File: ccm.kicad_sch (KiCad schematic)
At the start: 27 parts, among them J3 Conn_01x04_Socket, J4 Conn_01x04_Socket, J5 Conn_01x04_Socket, J6 Conn_01x02_Socket, J7 Conn_01x02_Socket, J8 Conn_01x04_Socket, Q1 IRLZ34N, U1 Teensy4.1, U2 PAM8302AAY, U3 SN65HVD230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

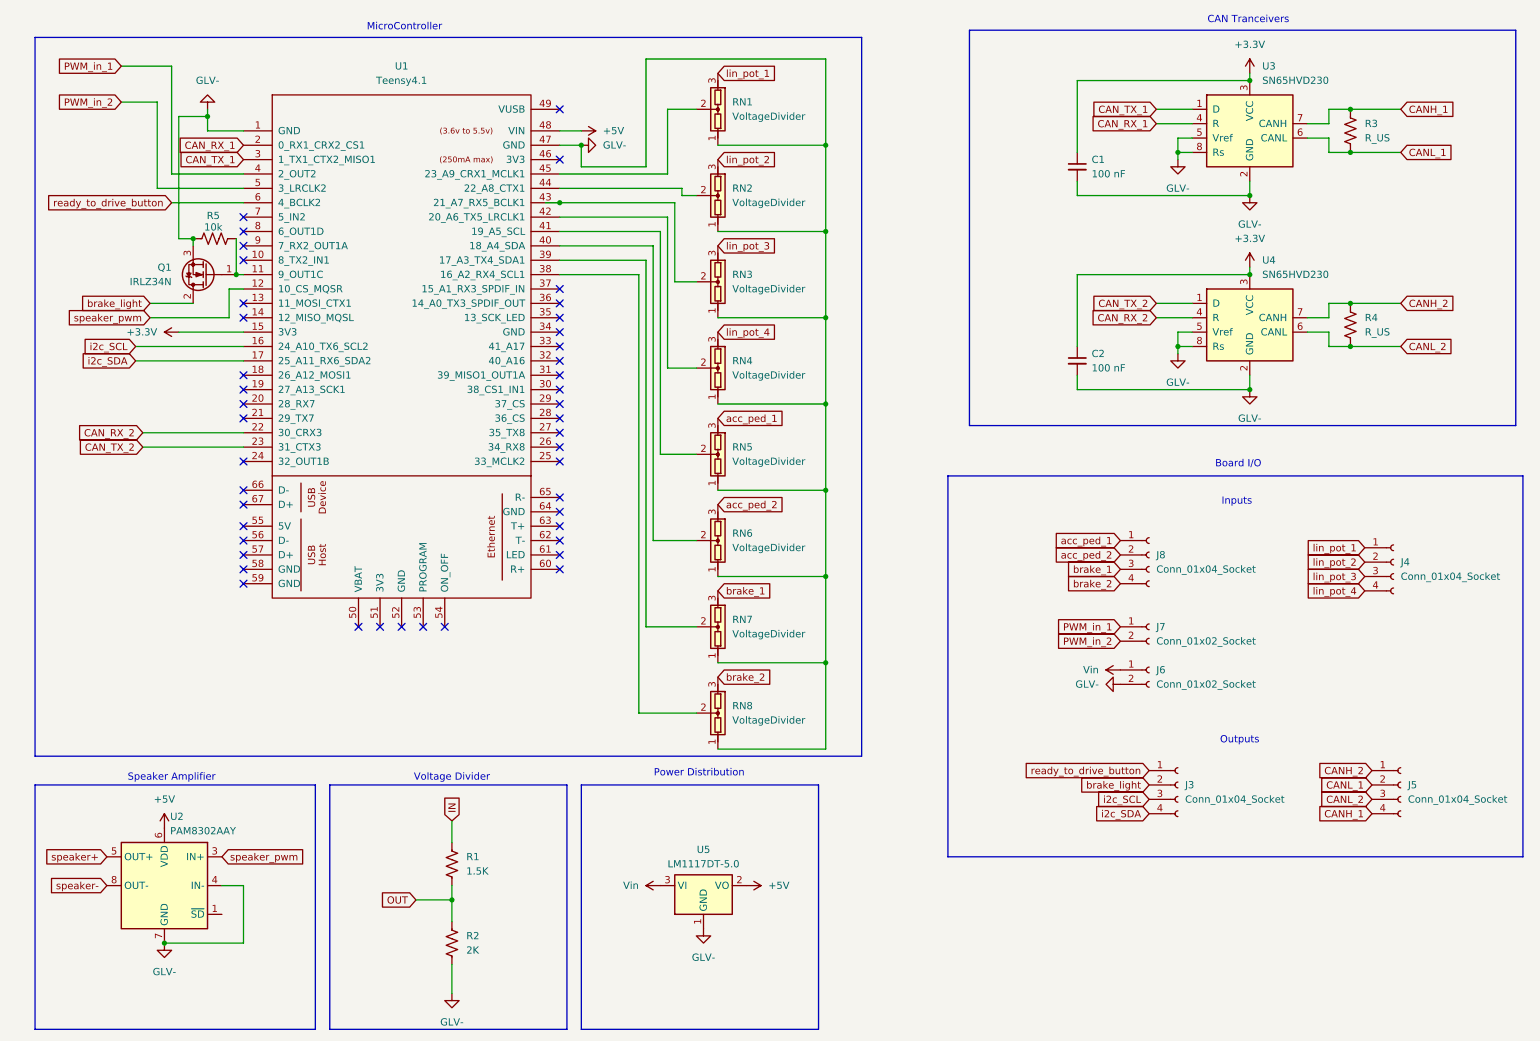
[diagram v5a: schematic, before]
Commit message: changed voltage divider to use 2 resistors
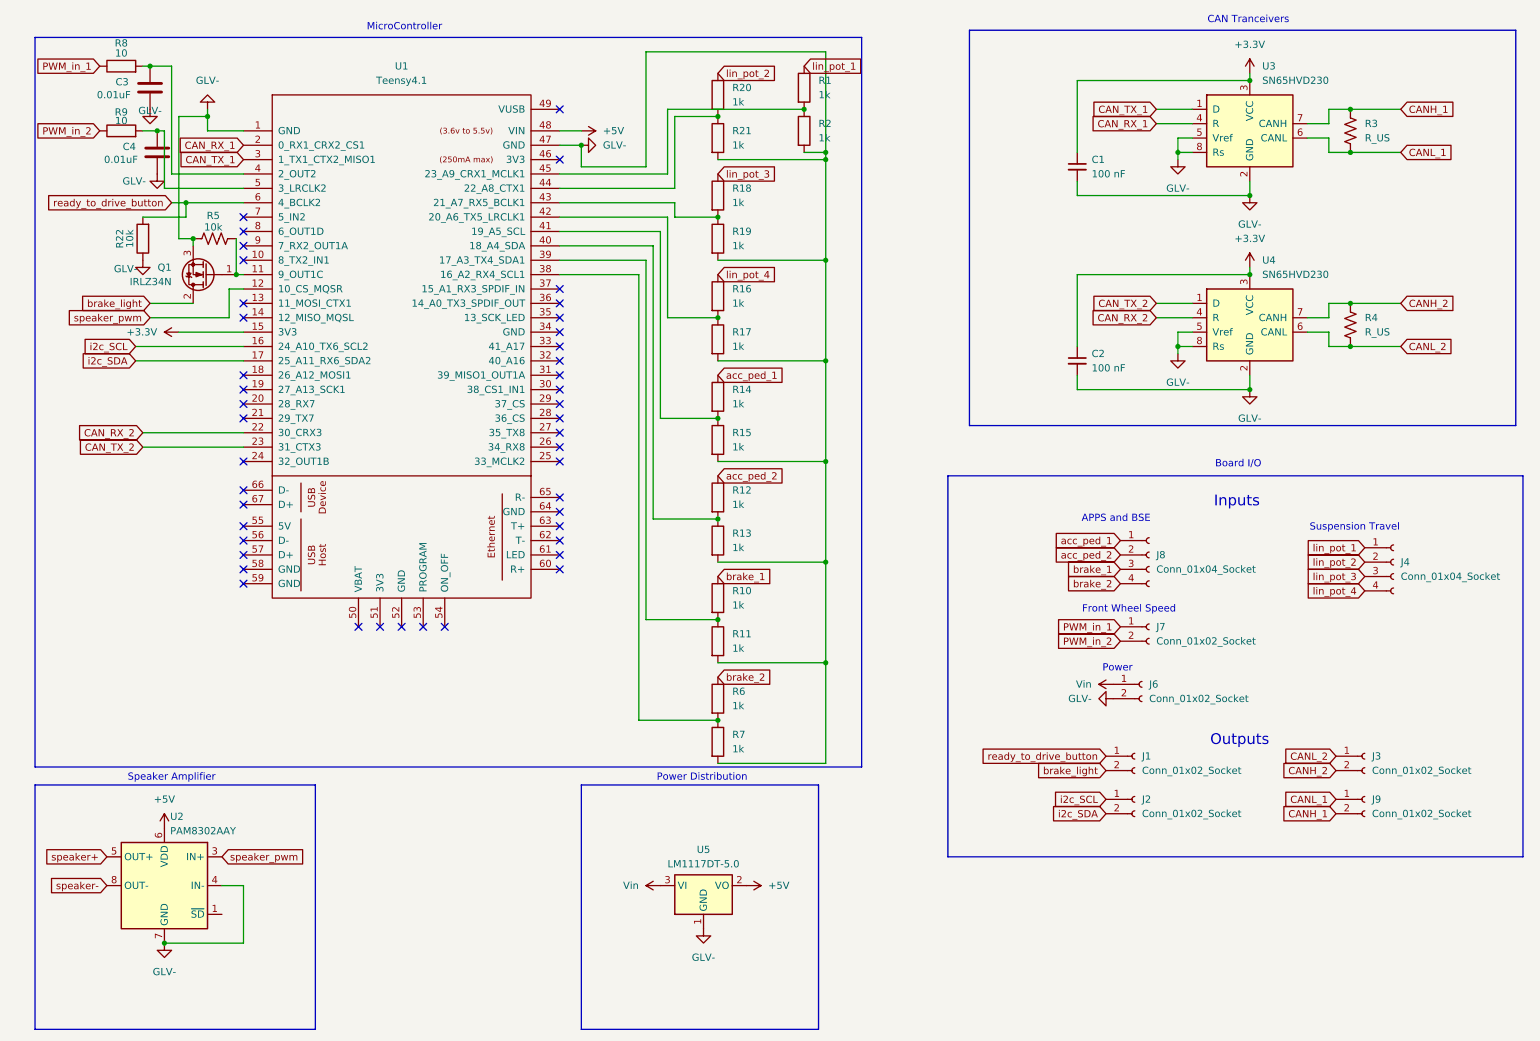
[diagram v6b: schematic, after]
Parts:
- removed J3, J5: Conn_01x04_Socket, Connector_Molex:Molex_Mini-Fit_Jr_5566-04A2_2x02_P4.20mm_Vertical, symbol Connector:Conn_01x04_Socket
- removed R1: 1.5K, symbol Device:R_US
- removed R2: 2K, symbol Device:R_US
- removed RN1, RN2, RN3, RN4, RN5, RN6, RN7, RN8: VoltageDivider, voltagedivider:Voltage_Divider, symbol Device:VoltageDivider
- added C3, C4: 0.01uF, Capacitor_SMD:C_0805_2012Metric, symbol Device:C
- added J1, J2, J3, J9: Conn_01x02_Socket, Connector_Molex:Molex_Mini-Fit_Jr_5566-02A2_2x01_P4.20mm_Vertical, symbol Connector:Conn_01x02_Socket
- added R1, R10, R11, R12, R13, R14, R15, R16, R17, R18, R19, R2, R20, R21, R6, R7: 1k, Resistor_SMD:R_0805_2012Metric, symbol Device:R
- added R22: 10k, Resistor_SMD:R_0805_2012Metric, symbol Device:R
- added R8, R9: 10, Resistor_SMD:R_0805_2012Metric, symbol Device:R
- C1, C2: footprint (none) -> Capacitor_SMD:C_0805_2012Metric
- R3, R4: footprint (none) -> Resistor_SMD:R_0805_2012Metric
- R5: footprint Resistor_SMD:R_0805_2012Metric_Pad1.20x1.40mm_HandSolder -> Resistor_SMD:R_0805_2012Metric
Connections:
- net CANH_1: now also J9.2 (Pin_2)
- net CANH_2: now also J3.2 (Pin_2)
- net CANL_1: now also J9.1 (Pin_1)
- net CANL_2: now also J3.1 (Pin_1)
- net GLV-: now also C3.2, C4.2, R11.2, R13.2, R15.2, R17.2, R19.2, R2.2, R21.2, R22.1, R7.2
- net PWM_in_1: now also R8.1; no longer U1.4 (2_OUT2)
- net PWM_in_2: now also R9.1; no longer U1.5 (3_LRCLK2)
- net acc_ped_1: now also R14.1
- net acc_ped_2: now also R12.1
- net brake_1: now also R10.1
- net brake_2: now also R6.1
- net brake_light: now also J1.2 (Pin_2)
- net i2c_SCL: now also J2.1 (Pin_1)
- net i2c_SDA: now also J2.2 (Pin_2)
- net lin_pot_1: now also R1.1
- net lin_pot_2: now also R20.1
- net lin_pot_3: now also R18.1
- net lin_pot_4: now also R16.1
- net ready_to_drive_button: now also J1.1 (Pin_1), R22.2
- net at U1.42 (20_A6_TX5_LRCLK1): now also R16.2, R17.1
- net at U1.40 (18_A4_SDA): now also R12.2, R13.1
- net at U1.43 (21_A7_RX5_BCLK1): now also R18.2, R19.1
- net at U1.41 (19_A5_SCL): now also R14.2, R15.1
- net at U1.44 (22_A8_CTX1): now also R20.2, R21.1
- net at U1.39 (17_A3_TX4_SDA1): now also R10.2, R11.1
- net at U1.38 (16_A2_RX4_SCL1): now also R6.2, R7.1
- net at U1.45 (23_A9_CRX1_MCLK1): now also R1.2, R2.1
- new net: C3.1, R8.2, U1.4 (2_OUT2)
- new net: C4.1, R9.2, U1.5 (3_LRCLK2)
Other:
- note added: "APPS and BSE"
- note added: "Front Wheel Speed"
- note added: "Power"
- note added: "Suspension Travel"
- note removed: "Voltage Divider"
- moved on the sheet: J6

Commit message: right side routed
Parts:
- added C5, C6: 100 nF, Capacitor_SMD:C_0805_2012Metric, symbol Device:C_Small
- added J10, J5: Conn_01x02_Socket, Connector_Molex:Molex_Mini-Fit_Jr_5566-02A2_2x01_P4.20mm_Vertical, symbol Connector:Conn_01x02_Socket
- added R23, R24: 1k, Resistor_SMD:R_0805_2012Metric, symbol Device:R
- added R25, R26: 60, Resistor_SMD:R_0805_2012Metric, symbol Device:R_US
- R3, R4: value R_US -> 60
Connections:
- net CANL_1: now also R25.2; no longer R3.2
- net CANL_2: now also R26.2; no longer R4.2
- net GLV-: now also C5.2, C6.2, R24.2
- net acc_ped_1: now also J8.4 (Pin_4); no longer J8.1 (Pin_1)
- net acc_ped_2: now also J8.3 (Pin_3); no longer J8.2 (Pin_2)
- net brake_1: now also J8.2 (Pin_2); no longer J8.3 (Pin_3)
- net brake_2: now also J8.1 (Pin_1); no longer J8.4 (Pin_4)
- net lin_pot_1: now also J4.4 (Pin_4); no longer J4.1 (Pin_1)
- net lin_pot_2: now also J4.3 (Pin_3); no longer J4.2 (Pin_2)
- net lin_pot_3: now also J4.2 (Pin_2); no longer J4.3 (Pin_3)
- net lin_pot_4: now also J4.1 (Pin_1); no longer J4.4 (Pin_4)
- net speaker+: now also J10.1 (Pin_1)
- net speaker-: now also J10.2 (Pin_2)
- net at U1.37 (15_A1_RX3_SPDIF_IN): now also R23.2, R24.1
- new net: C6.1, R26.1, R4.2
- new net: C5.1, R25.1, R3.2
- new net rtm_sound: J5.1 (Pin_1), R23.1
- no-connect marks 44 -> 45
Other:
- moved on the sheet: C3, C4, J3, J9, Q1, R22, R3, R5, R8, R9, U1

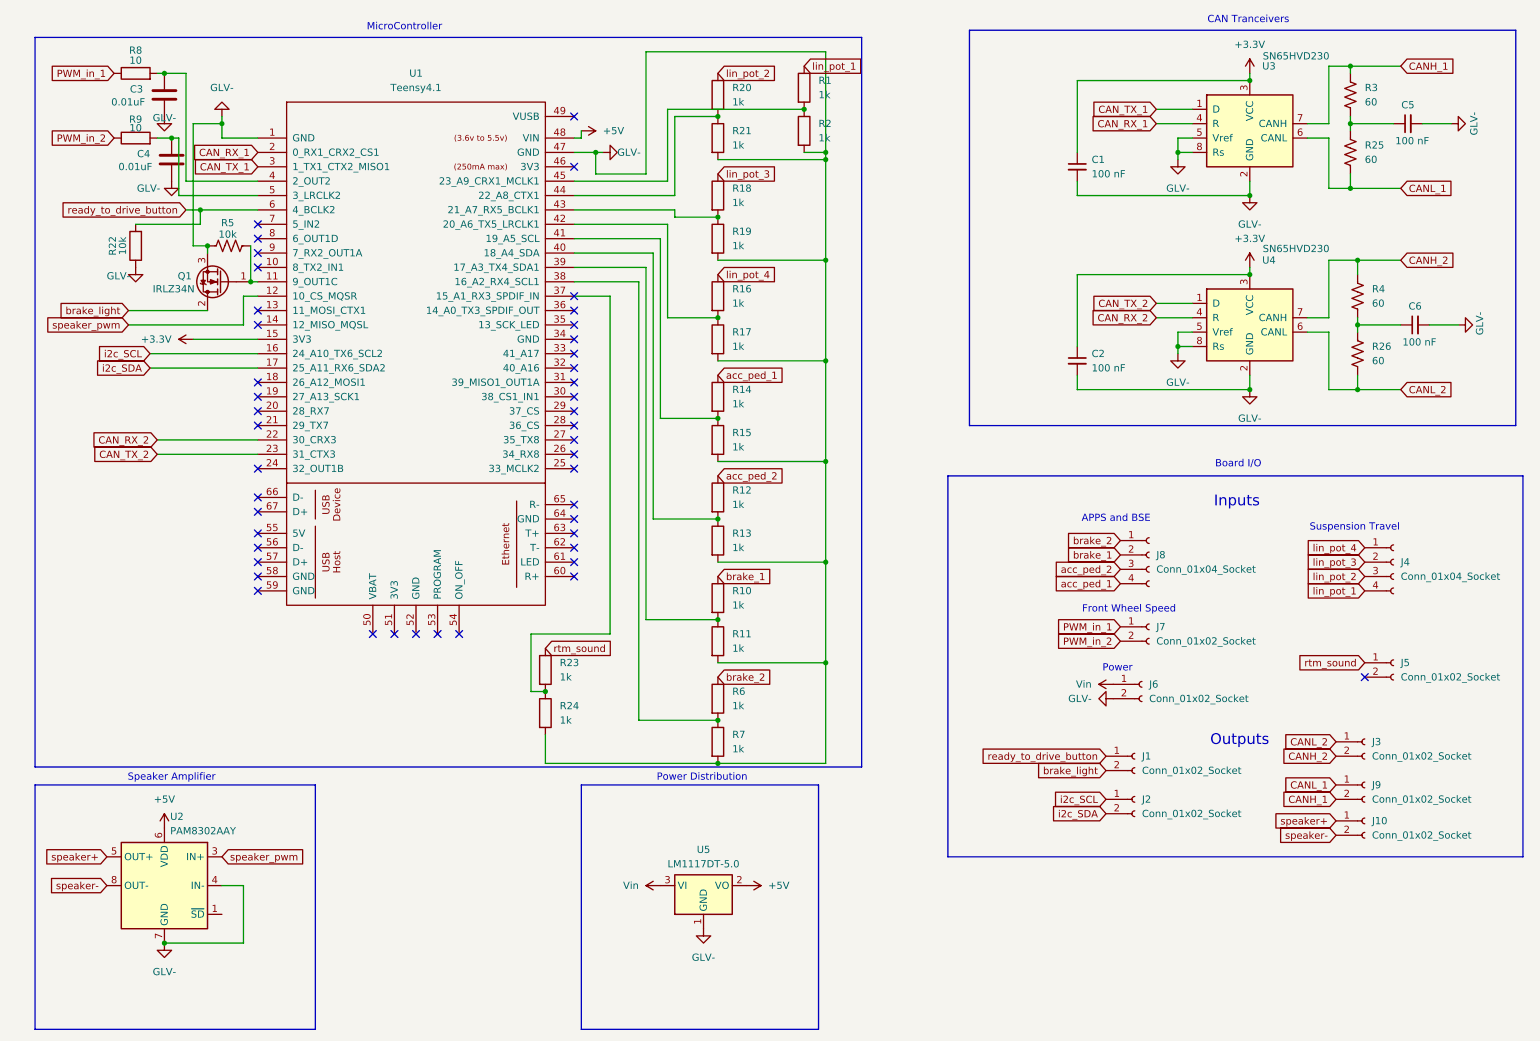
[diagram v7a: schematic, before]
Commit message: added serial resistors to CAN tranciever
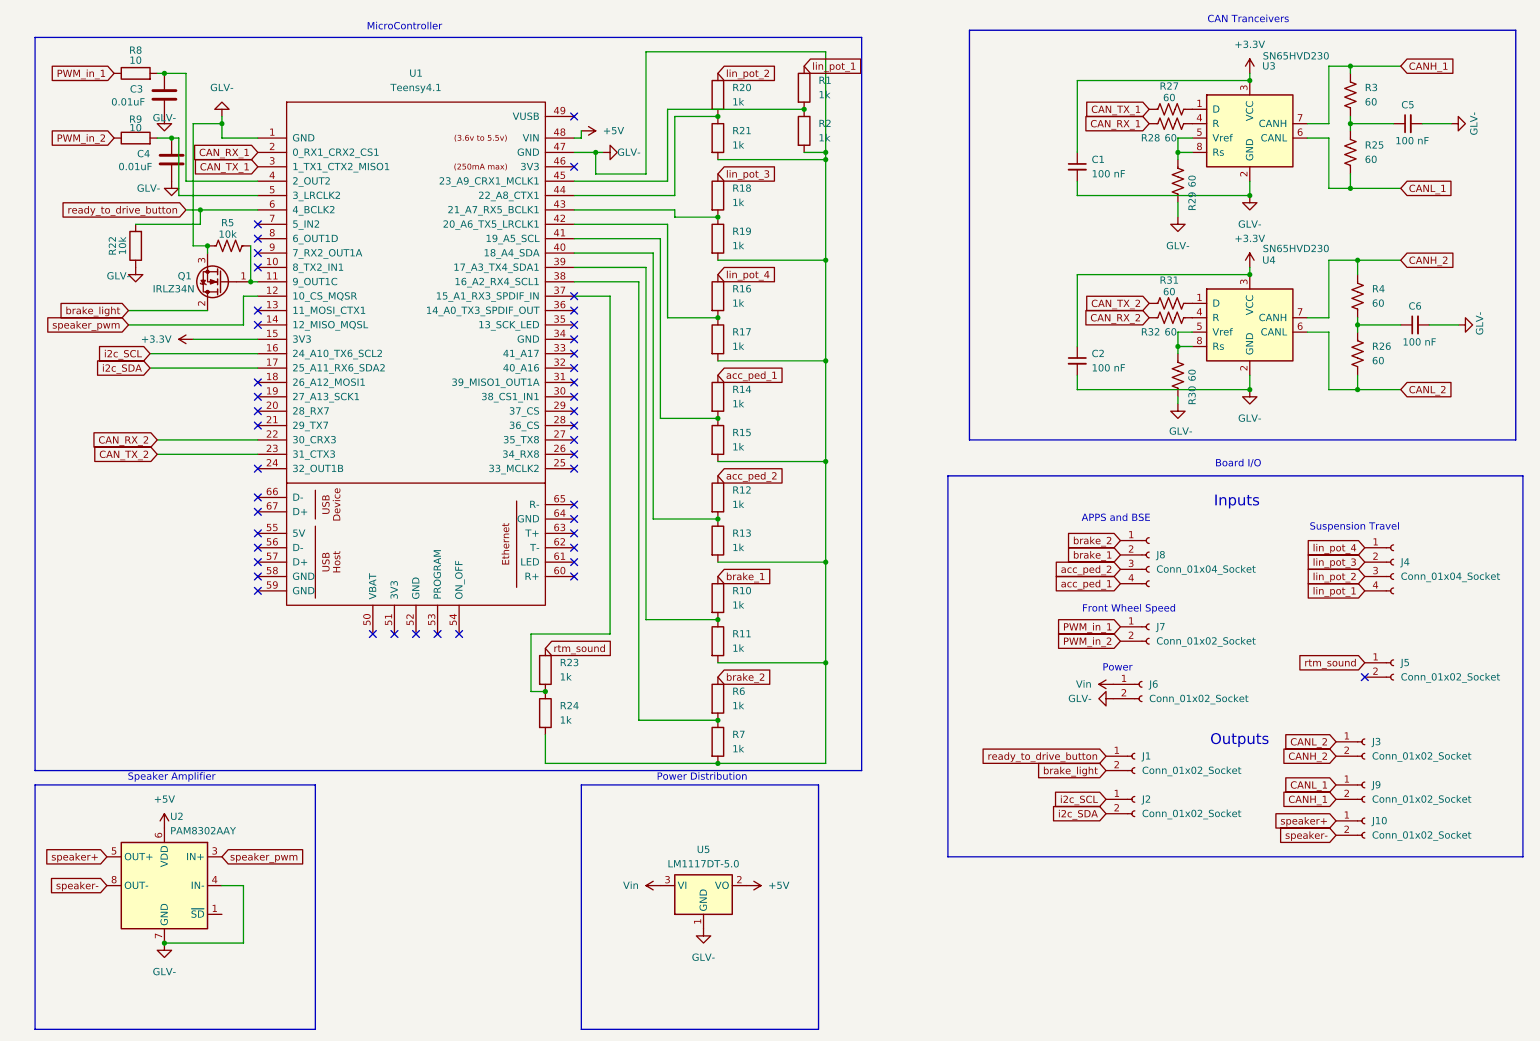
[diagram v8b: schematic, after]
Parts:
- added R27, R28, R29, R30, R31, R32: 60, Resistor_SMD:R_0805_2012Metric, symbol Device:R_US
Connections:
- net CAN_RX_1: now also R28.1; no longer U3.4 (R)
- net CAN_RX_2: now also R32.1; no longer U4.4 (R)
- net CAN_TX_1: now also R27.1; no longer U3.1 (D)
- net CAN_TX_2: now also R31.1; no longer U4.1 (D)
- net GLV-: now also R29.1, R30.1; no longer U3.5 (Vref), U3.8 (Rs), U4.5 (Vref), U4.8 (Rs)
- new net: R32.2, U4.4 (R)
- new net: R28.2, U3.4 (R)
- new net: R31.2, U4.1 (D)
- new net: R30.2, U4.5 (Vref), U4.8 (Rs)
- new net: R29.2, U3.5 (Vref), U3.8 (Rs)
- new net: R27.2, U3.1 (D)
